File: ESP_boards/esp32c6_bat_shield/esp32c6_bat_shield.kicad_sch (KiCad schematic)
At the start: 1 part, among them U1 ESP32-C6-WROOM-1-N4

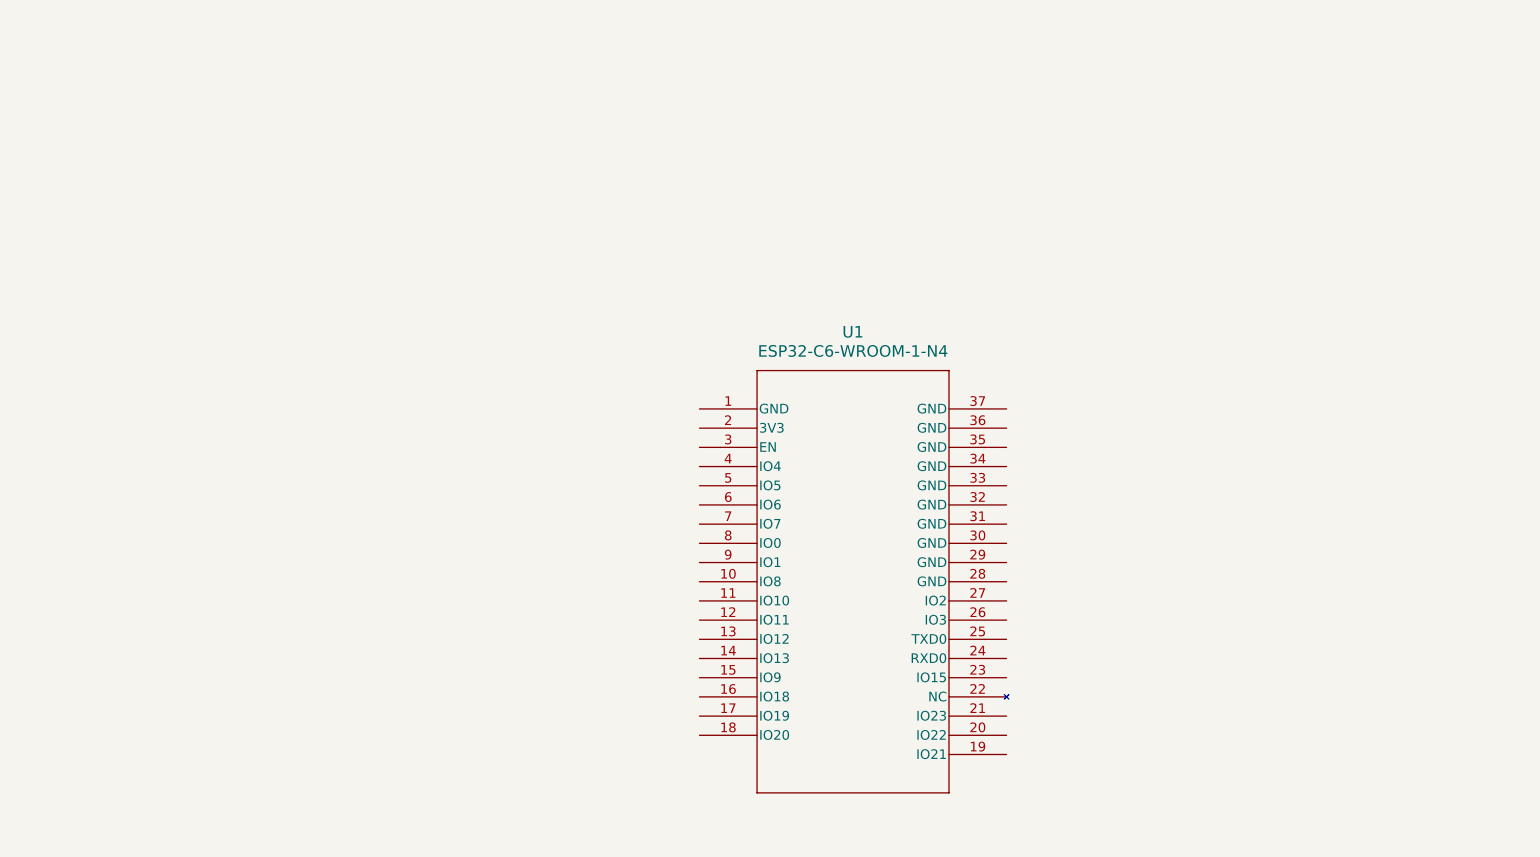
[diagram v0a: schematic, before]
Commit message: Added USB-C connector
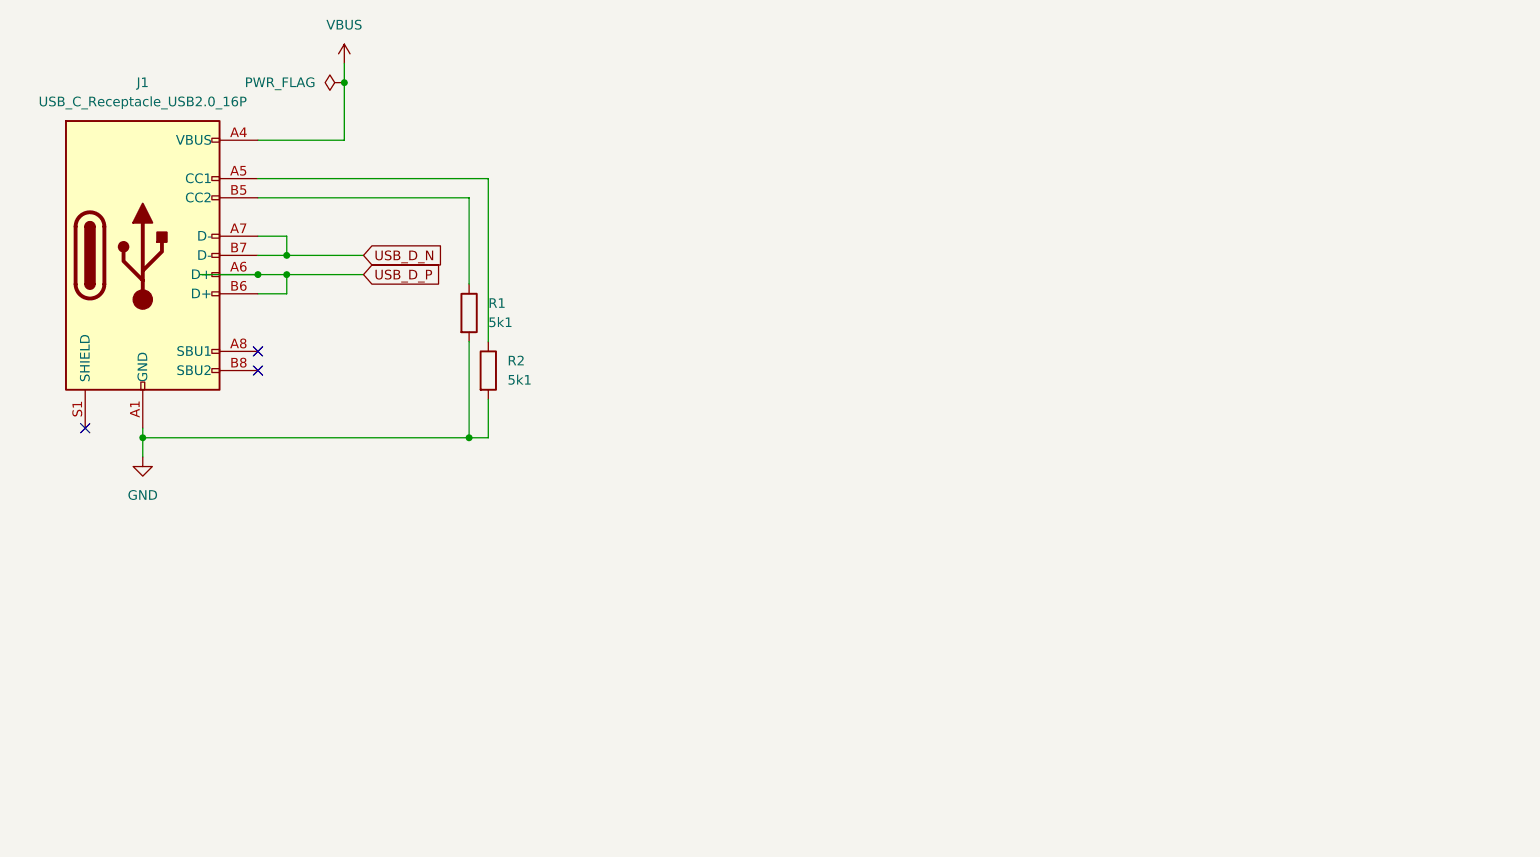
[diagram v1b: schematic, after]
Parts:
- removed U1: ESP32-C6-WROOM-1-N4, MCU_espressif_moma:ESP32-C6-WROOM-1_EXP_MOD28, symbol MCU_espressif_moma:ESP32-C6-WROOM-1-N4
- added J1: USB_C_Receptacle_USB2.0_16P, Connector_USB:USB_C_Receptacle_GCT_USB4105-xx-A_16P_TopMnt_Horizontal, symbol Connector:USB_C_Receptacle_USB2.0_16P
- added R1, R2: 5k1, Resistor_SMD:R_0603_1608Metric, symbol Device:R
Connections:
- new net: J1.A5 (CC1), R2.1
- new net: J1.B5 (CC2), R1.1
- new net GND: J1.A1 (GND), J1.A12 (GND), J1.B1 (GND), J1.B12 (GND), R1.2, R2.2
- new net USB_D_N: J1.A7 (D-), J1.B7 (D-)
- new net USB_D_P: J1.A6 (D+), J1.B6 (D+)
- new net VBUS: J1.A4 (VBUS), J1.A9 (VBUS), J1.B4 (VBUS), J1.B9 (VBUS)
- no-connect marks 0 -> 3

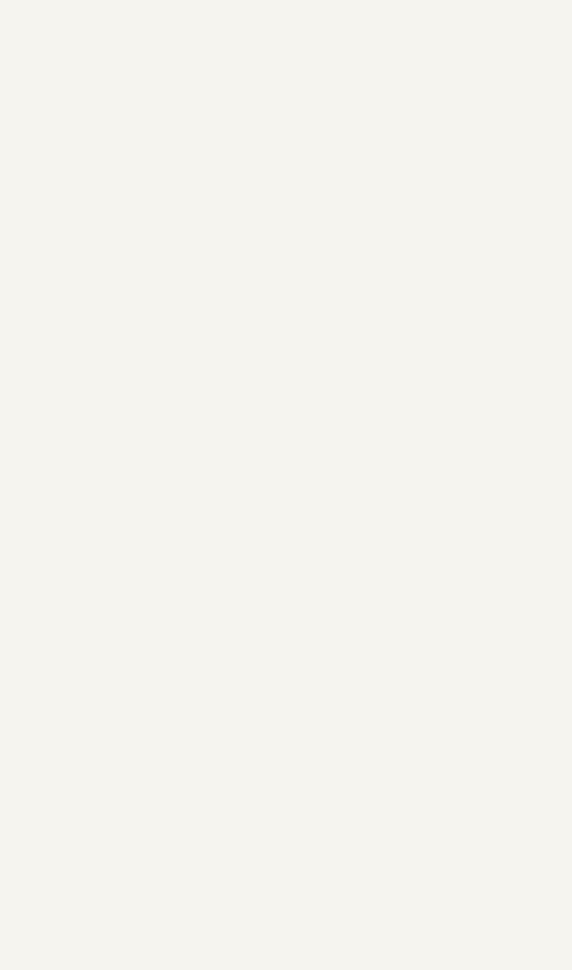
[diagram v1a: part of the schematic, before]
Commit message: Added esp32c6-mini to library
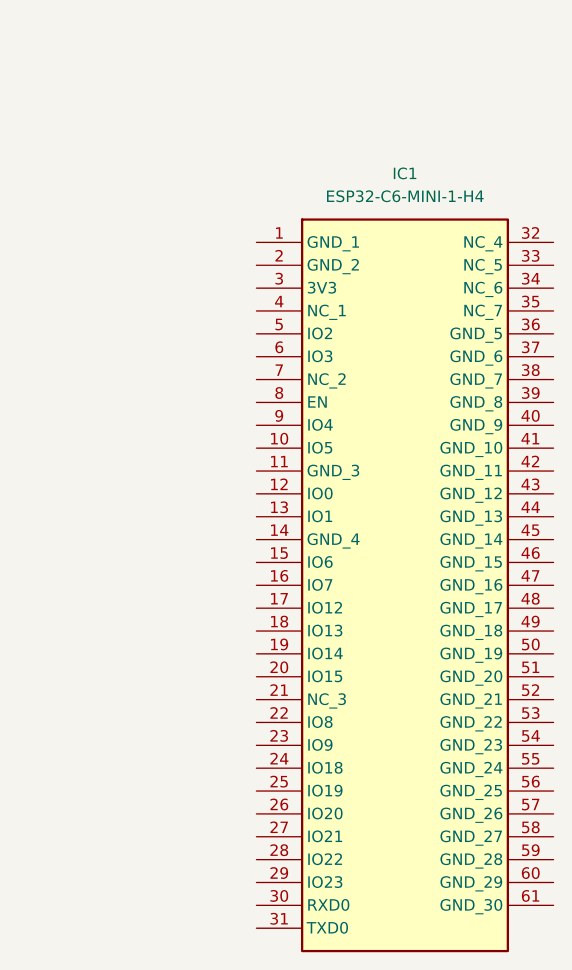
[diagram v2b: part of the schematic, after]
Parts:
- added IC1: ESP32-C6-MINI-1-H4, ESP32C6MINI1H4, symbol MCU_espressif_moma:ESP32-C6-MINI-1-H4
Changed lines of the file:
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@@
+	)
+	(symbol
+		(lib_id "MCU_espressif_moma:ESP32-C6-MINI-1-H4")
+		(at 199.39 46.99 0)
+		(unit 1)
+		(exclude_from_sim no)
+		(in_bom yes)
+		(on_board yes)
+		(dnp no)
+		(fields_autoplaced yes)
+		(property "Reference" "IC1"
+			(at 215.9 39.37 0)
+			(effects
+				(font
+					(size 1.27 1.27)
+				)
+			)
+		)
+		(property "Value" "ESP32-C6-MINI-1-H4"
+			(at 215.9 41.91 0)
+			(effects
+				(font
+					(size 1.27 1.27)
+				)
+			)
+		)
+		(property "Footprint" "ESP32C6MINI1H4"
+			(at 228.6 141.91 0)
+			(effects
+				(font
+					(size 1.27 1.27)
+				)
+				(justify left top)
+				(hide yes)
+			)
+		)
+		(property "Datasheet" "https://www.espressif.com/sites/default/files/documentation/esp32-c6-mini-1_mini-1u_datasheet_en.pdf"
+			(at 228.6 241.91 0)
+			(effects
+				(font
+					(size 1.27 1.27)
+				)
+				(justify left top)
+				(hide yes)
+			)
+		)
+		(property "Description" "Multiprotocol Modules ESP32-C6 Module, supports Wi-Fi 6 in 2.4 GHz band, Bluetooth 5, Zigbee 3.0 and Thread - -40 to 85C"
+			(at 199.39 46.99 0)
+			(effects
+				(font
+					(size 1.27 1.27)
+				)
+				(hide yes)
+			)
+		)
+		(property "Height" "2.55"
+			(at 228.6 441.91 0)
+			(effects
+				(font
+					(size 1.27 1.27)
+				)
+				(justify left top)
+				(hide yes)
+			)
+		)
+		(property "Mouser Part Number" "356-ESP32C6MINI1-H4"
+			(at 228.6 541.91 0)
+			(effects
+				(font
+					(size 1.27 1.27)
+				)
+				(justify left top)
+				(hide yes)
+			)
+		)
+		(property "Mouser Price/Stock" "https://www.mouser.co.uk/ProductDetail/Espressif-Systems/ESP32-C6-MINI-1-H4?qs=Jm2GQyTW%2Fbgg5ClQiAJNHw%3D%3D"
+			(at 228.6 641.91 0)
+			(effects
+				(font
+					(size 1.27 1.27)
+				)
+				(justify left top)
+				(hide yes)
+			)
+		)
+		(property "Manufacturer_Name" "Espressif Systems"
+			(at 228.6 741.91 0)
+			(effects
+				(font
+					(size 1.27 1.27)
+				)
+				(justify left top)
+				(hide yes)
+			)
+		)
+		(property "Manufacturer_Part_Number" "ESP32-C6-MINI-1-H4"
+			(at 228.6 841.91 0)
+			(effects
+				(font
+					(size 1.27 1.27)
+				)
+				(justify left top)
+				(hide yes)
+			)
+		)
+		(pin "56"
+		)
+		(pin "36"
+		)
+		(pin "41"
+		)
+		(pin "11"
+		)
+		(pin "43"
+		)
+		(pin "26"
+		)
+		(pin "25"
+		)
+		(pin "60"
+		)
+		(pin "4"
+		)
+		(pin "59"
+		)
+		(pin "42"
+		)
+		(pin "34"
+		)
+		(pin "27"
+		)
+		(pin "54"
+		)
+		(pin "17"
+		)
+		(pin "2"
+		)
+		(pin "1"
+		)
+		(pin "7"
+		)
+		(pin "44"
+		)
+		(pin "37"
+		)
+		(pin "40"
+		)
+		(pin "51"
+		)
+		(pin "55"
+		)
+		(pin "30"
+		)
+		(pin "6"
+		)
+		(pin "18"
+		)
+		(pin "9"
+		)
+		(pin "45"
+		)
+		(pin "8"
+		)
+		(pin "5"
+		)
+		(pin "14"
+		)
+		(pin "20"
+		)
+		(pin "38"
+		)
+		(pin "47"
+		)
+		(pin "12"
+		)
+		(pin "39"
+		)
+		(pin "61"
+		)
+		(pin "28"
+		)
+		(pin "52"
+		)
+		(pin "19"
+		)
+		(pin "57"
+		)
+		(pin "21"
+		)
+		(pin "33"
+		)
+		(pin "13"
+		)
+		(pin "53"
+		)
+		(pin "48"
+		)
+		(pin "58"
+		)
+		(pin "16"
+		)
+		(pin "46"
+		)
+		(pin "29"
+		)
+		(pin "22"
+		)
+		(pin "24"
+		)
+		(pin "23"
+		)
+		(pin "10"
+		)
+		(pin "3"
+		)
+		(pin "49"
+		)
+		(pin "31"
+		)
+		(pin "35"
+		)
+		(pin "15"
+		)
+		(pin "50"
+		)
+		(pin "32"
+		)
+		(instances
+			(project ""
+				(path "/3c91fec2-0062-4c1f-a7ef-5bde720f139e"
+					(reference "IC1")
+					(unit 1)
+				)
+			)
+		)
 	)
 	(symbol
